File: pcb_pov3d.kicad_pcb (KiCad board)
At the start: 2 copper layers, 92 parts, among them P1 CONN_4X2, P2 CONN_6, P3 MICRO-SD, P4 CONN_2, P5 KNUSB, P6 CONN_12, U1 TLC5955, U2 TLC5955, U3 TLC5955, U4 STM32F40X_LQFP64, U5 US4881_HALL, U6 LP38691, X1 CRYSTAL

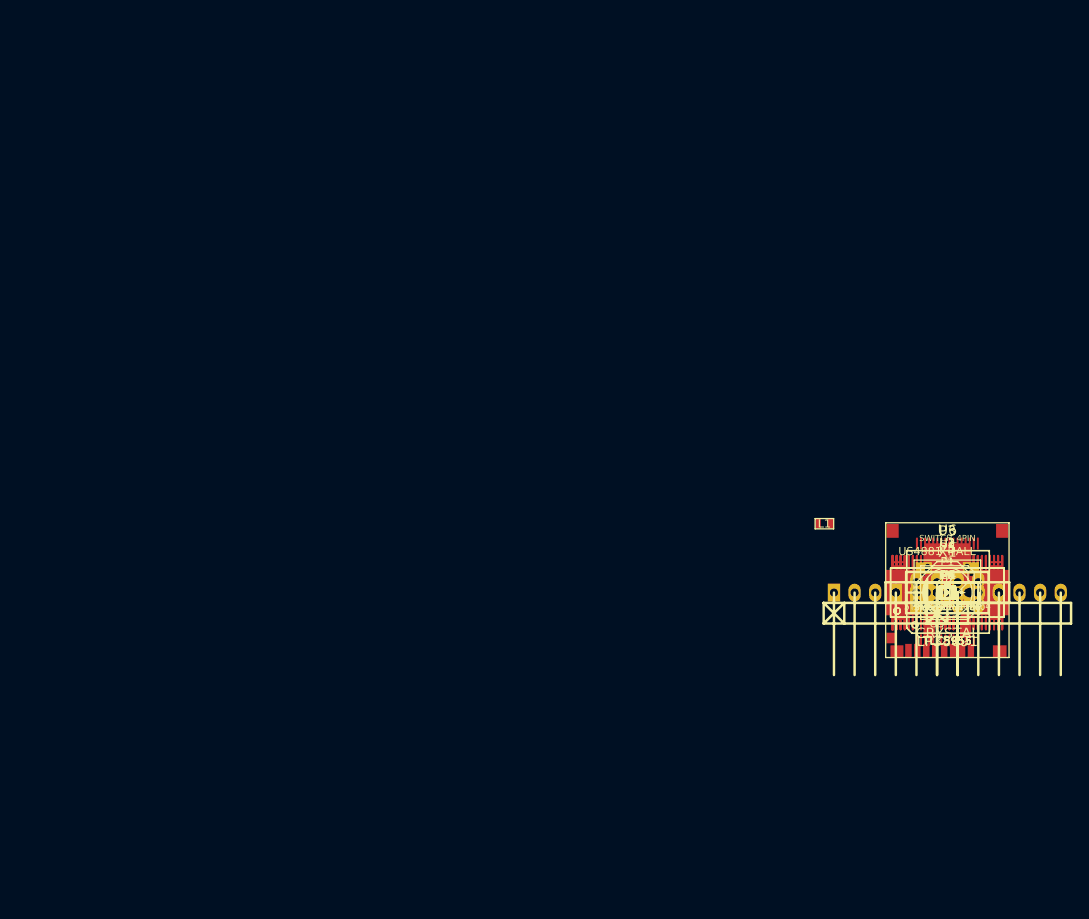
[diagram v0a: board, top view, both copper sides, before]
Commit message: Place RGB LEDs in the computed pattern for 3D POV effect.
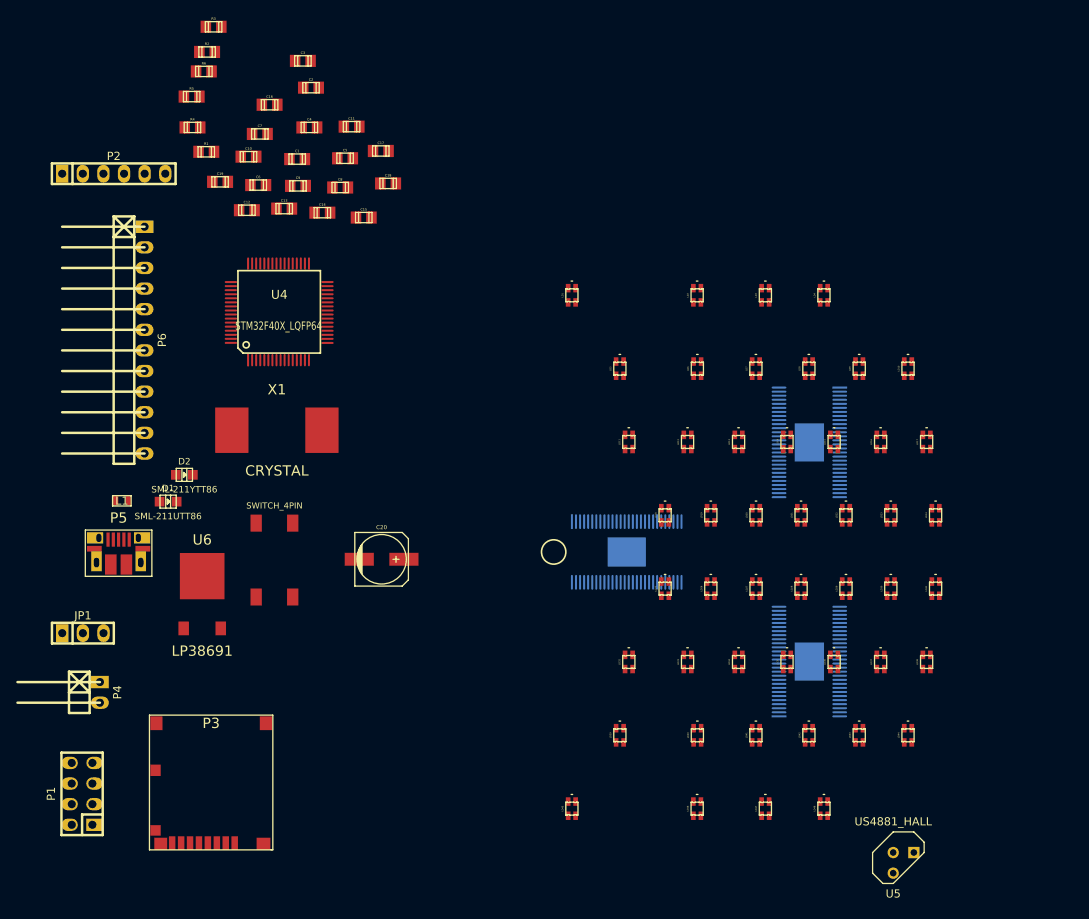
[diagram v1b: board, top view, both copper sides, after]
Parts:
- U1, U2, U3: moved to B.Cu
- moved P2 114.9 mm to (45.8, 53.4)
- moved R3 114.2 mm to (58.1, 35.3)
- moved R2 112.9 mm to (57.3, 38.4)
- moved R6 111.9 mm to (56.9, 40.8)
- moved R5 111.4 mm to (55.4, 43.9)
- moved P1 109.4 mm to (41.9, 129.8), turned to 90 degrees
- moved R4 109.2 mm to (55.5, 47.7)
- moved JP1 106.6 mm to (42.0, 110.0)
- moved R1 106.2 mm to (57.2, 50.7)
- moved P4 105.1 mm to (44.1, 117.3), turned to 270 degrees
- moved P6 103.7 mm to (49.6, 73.9), turned to 270 degrees
- moved C3 102.9 mm to (69.1, 39.5)
- moved C19 102.9 mm to (58.9, 54.4)
- moved C16 102.9 mm to (65.0, 44.9)
- moved P5 102.2 mm to (46.4, 101.3)
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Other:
- copper layers 2 -> 4
- net class Default: clearance 0.254 -> 0.2032; trace_width 0.254 -> 0.2032; via_dia 0.889 -> 0.635; via_drill 0.635 -> 0.3048
- net class Inner added: clearance 0.2032, trace_width 0.254, via_dia 0.635, via_drill 0.3048
- net class Tight added: clearance 0.1524, trace_width 0.1524, via_dia 0.635, via_drill 0.3048
- rule trace_clearance: 0.254 -> 0.2032
- rule trace_min: 0.254 -> 0.1524
- rule via_min_drill: 0.508 -> 0.3048
- rule via_min_size: 0.889 -> 0.635

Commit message: Assignment of LEDs to TLC5955 outputs.
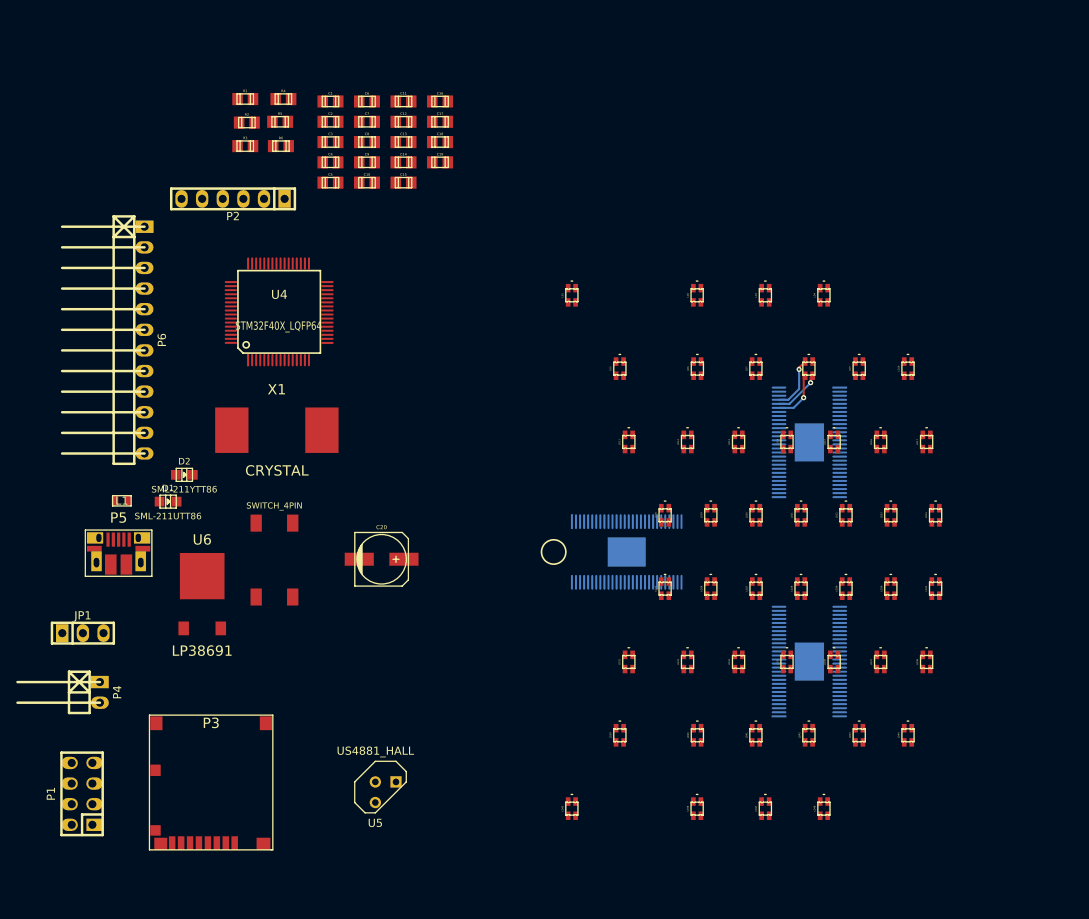
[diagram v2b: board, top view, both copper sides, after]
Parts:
- moved U5 64.4 mm to (79.3, 129.6)
- moved C19 27.2 mm to (86.0, 52.0)
- moved C12 22.2 mm to (81.5, 47.0)
- moved C16 21.0 mm to (86.0, 44.5)
- moved C6 16.9 mm to (77.0, 44.5)
- moved C13 16.8 mm to (81.5, 49.5)
- moved R3 15.2 mm to (62.0, 50.0)
- moved P2 15.0 mm to (60.5, 56.5), turned to 180 degrees
- moved C10 14.9 mm to (77.0, 54.5)
- moved C7 13.3 mm to (77.0, 47.0)
- moved R6 13.2 mm to (66.4, 50.0)
- moved C14 11.8 mm to (81.5, 52.0)
- moved R4 11.7 mm to (66.7, 44.2)
- moved R5 11.3 mm to (66.3, 47.0)
- moved C3 10.6 mm to (72.5, 49.5)
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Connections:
- U1 pad 10: /LEDs/t1o5b -> /LEDs/led15b
- U1 pad 11: /LEDs/t1o5r -> /LEDs/led15r
- U1 pad 12: /LEDs/t1o5g -> /LEDs/led15g
- U1 pad 13: /LEDs/t1o1b -> /LEDs/led16b
- U1 pad 14: /LEDs/t1o1r -> /LEDs/led16r
- U1 pad 15: /LEDs/t1o1g -> /LEDs/led16g
- U1 pad 16: /LEDs/t1o2b -> /LEDs/led17b
- U1 pad 17: /LEDs/t1o2r -> /LEDs/led17r
- U1 pad 18: /LEDs/t1o2g -> /LEDs/led17g
- U1 pad 19: /LEDs/t1o6b -> /LEDs/led24b
- U1 pad 20: /LEDs/t1o6r -> /LEDs/led24r
- U1 pad 21: /LEDs/t1o6g -> /LEDs/led24g
- U1 pad 22: /LEDs/t1o3b -> /LEDs/led23b
- U1 pad 23: /LEDs/t1o3r -> /LEDs/led23r
- U1 pad 24: /LEDs/t1o3g -> /LEDs/led23g
- U1 pad 25: /LEDs/t1o7b -> /LEDs/led22b
- U1 pad 26: /LEDs/t1o7r -> /LEDs/led22r
- U1 pad 27: /LEDs/t1o7g -> /LEDs/led22g
- U1 pad 30: /LEDs/t1o11g -> /LEDs/led21g
- U1 pad 31: /LEDs/t1o11r -> /LEDs/led21r
- U1 pad 32: /LEDs/t1o11b -> /LEDs/led21b
- U1 pad 33: /LEDs/t1o15g -> /LEDs/led20g
- U1 pad 34: /LEDs/t1o15r -> /LEDs/led20r
- U1 pad 35: /LEDs/t1o15b -> /LEDs/led20b
- U1 pad 36: /LEDs/t1o10g -> /LEDs/led13g
- U1 pad 37: /LEDs/t1o10r -> /LEDs/led13r
- U1 pad 38: /LEDs/t1o10b -> /LEDs/led13b
- U1 pad 39: /LEDs/t1o14g -> /LEDs/led7g
- U1 pad 4: /LEDs/t1o4b -> /LEDs/led9b
- U1 pad 40: /LEDs/t1o14r -> /LEDs/led7r
- U1 pad 41: /LEDs/t1o14b -> /LEDs/led7b
- U1 pad 42: /LEDs/t1o13g -> /LEDs/led14g
- U1 pad 43: /LEDs/t1o13r -> /LEDs/led14r
- U1 pad 44: /LEDs/t1o13b -> /LEDs/led14b
- U1 pad 45: /LEDs/t1o9g -> /LEDs/led4g
- U1 pad 46: /LEDs/t1o9r -> /LEDs/led4r
- U1 pad 47: /LEDs/t1o9b -> /LEDs/led4b
- U1 pad 48: /LEDs/t1o12g -> /LEDs/led3g
- U1 pad 49: /LEDs/t1o12r -> /LEDs/led3r
- U1 pad 5: /LEDs/t1o4r -> /LEDs/led9r
- U1 pad 50: /LEDs/t1o12b -> /LEDs/led3b
- U1 pad 51: /LEDs/t1o8g -> /LEDs/led8g
- U1 pad 52: /LEDs/t1o8r -> /LEDs/led8r
- U1 pad 53: /LEDs/t1o8b -> /LEDs/led8b
- U1 pad 6: /LEDs/t1o4g -> /LEDs/led9g
- U1 pad 7: /LEDs/t1o0b -> /LEDs/led10b
- U1 pad 8: /LEDs/t1o0r -> /LEDs/led10r
- U1 pad 9: /LEDs/t1o0g -> /LEDs/led10g
- U2 pad 10: /LEDs/t2o5b -> /LEDs/led11b
- U2 pad 11: /LEDs/t2o5r -> /LEDs/led11r
- U2 pad 12: /LEDs/t2o5g -> /LEDs/led11g
- U2 pad 13: /LEDs/t2o1b -> /LEDs/led2b
- U2 pad 14: /LEDs/t2o1r -> /LEDs/led2r
- U2 pad 15: /LEDs/t2o1g -> /LEDs/led2g
- U2 pad 16: /LEDs/t2o2b -> /LEDs/led6b
- U2 pad 17: /LEDs/t2o2r -> /LEDs/led6r
- U2 pad 18: /LEDs/t2o2g -> /LEDs/led6g
- U2 pad 19: /LEDs/t2o6b -> /LEDs/led12b
- U2 pad 20: /LEDs/t2o6r -> /LEDs/led12r
- U2 pad 21: /LEDs/t2o6g -> /LEDs/led12g
- U2 pad 22: /LEDs/t2o3b -> /LEDs/led18b
- U2 pad 23: /LEDs/t2o3r -> /LEDs/led18r
- U2 pad 24: /LEDs/t2o3g -> /LEDs/led18g
- U2 pad 25: /LEDs/t2o7b -> /LEDs/led19b
- U2 pad 26: /LEDs/t2o7r -> /LEDs/led19r
- U2 pad 27: /LEDs/t2o7g -> /LEDs/led19g
- U2 pad 30: /LEDs/t2o11g -> /LEDs/led26g
- U2 pad 31: /LEDs/t2o11r -> /LEDs/led26r
- U2 pad 32: /LEDs/t2o11b -> /LEDs/led26b
- U2 pad 33: /LEDs/t2o15g -> /LEDs/led25g
- U2 pad 34: /LEDs/t2o15r -> /LEDs/led25r
- U2 pad 35: /LEDs/t2o15b -> /LEDs/led25b
- U2 pad 36: /LEDs/t2o10g -> /LEDs/led33g
- U2 pad 37: /LEDs/t2o10r -> /LEDs/led33r
- U2 pad 38: /LEDs/t2o10b -> /LEDs/led33b
- U2 pad 39: /LEDs/t2o14g -> /LEDs/led40g
- U2 pad 4: /LEDs/t2o4b -> /LEDs/led1b
- U2 pad 40: /LEDs/t2o14r -> /LEDs/led40r
- U2 pad 41: /LEDs/t2o14b -> /LEDs/led40b
- U2 pad 42: /LEDs/t2o13g -> /LEDs/led46g
- U2 pad 43: /LEDs/t2o13r -> /LEDs/led46r
- U2 pad 44: /LEDs/t2o13b -> /LEDs/led46b
- U2 pad 45: /LEDs/t2o9g -> /LEDs/led32g
- U2 pad 46: /LEDs/t2o9r -> /LEDs/led32r
- U2 pad 47: /LEDs/t2o9b -> /LEDs/led32b
- U2 pad 48: /LEDs/t2o12g -> /LEDs/led39g
- U2 pad 49: /LEDs/t2o12r -> /LEDs/led39r
- U2 pad 5: /LEDs/t2o4r -> /LEDs/led1r
- U2 pad 50: /LEDs/t2o12b -> /LEDs/led39b
- U2 pad 51: /LEDs/t2o8g -> /LEDs/led45g
- U2 pad 52: /LEDs/t2o8r -> /LEDs/led45r
- U2 pad 53: /LEDs/t2o8b -> /LEDs/led45b
- U2 pad 6: /LEDs/t2o4g -> /LEDs/led1g
- U2 pad 7: /LEDs/t2o0b -> /LEDs/led5b
- U2 pad 8: /LEDs/t2o0r -> /LEDs/led5r
- U2 pad 9: /LEDs/t2o0g -> /LEDs/led5g
- U3 pad 10: /LEDs/t3o5b -> /LEDs/led48b
- U3 pad 11: /LEDs/t3o5r -> /LEDs/led48r
- U3 pad 12: /LEDs/t3o5g -> /LEDs/led48g
- U3 pad 13: /LEDs/t3o1b -> /LEDs/led35b
- U3 pad 14: /LEDs/t3o1r -> /LEDs/led35r
- U3 pad 15: /LEDs/t3o1g -> /LEDs/led35g
- U3 pad 16: /LEDs/t3o2b -> /LEDs/led41b
- U3 pad 17: /LEDs/t3o2r -> /LEDs/led41r
- U3 pad 18: /LEDs/t3o2g -> /LEDs/led41g
- U3 pad 19: /LEDs/t3o6b -> /LEDs/led34b
- U3 pad 20: /LEDs/t3o6r -> /LEDs/led34r
- U3 pad 21: /LEDs/t3o6g -> /LEDs/led34g
- U3 pad 22: /LEDs/t3o3b -> /LEDs/led27b
- U3 pad 23: /LEDs/t3o3r -> /LEDs/led27r
- U3 pad 24: /LEDs/t3o3g -> /LEDs/led27g
- U3 pad 25: /LEDs/t3o7b -> /LEDs/led28b
- U3 pad 26: /LEDs/t3o7r -> /LEDs/led28r
- U3 pad 27: /LEDs/t3o7g -> /LEDs/led28g
- U3 pad 30: /LEDs/t3o11g -> /LEDs/led29g
- U3 pad 31: /LEDs/t3o11r -> /LEDs/led29r
- U3 pad 32: /LEDs/t3o11b -> /LEDs/led29b
- U3 pad 33: /LEDs/t3o15g -> /LEDs/led30g
- U3 pad 34: /LEDs/t3o15r -> /LEDs/led30r
- U3 pad 35: /LEDs/t3o15b -> /LEDs/led30b
- U3 pad 36: /LEDs/t3o10g -> /LEDs/led31g
- U3 pad 37: /LEDs/t3o10r -> /LEDs/led31r
- U3 pad 38: /LEDs/t3o10b -> /LEDs/led31b
- U3 pad 39: /LEDs/t3o14g -> /LEDs/led38g
- U3 pad 4: /LEDs/t3o4b -> /LEDs/led42b
- U3 pad 40: /LEDs/t3o14r -> /LEDs/led38r
- U3 pad 41: /LEDs/t3o14b -> /LEDs/led38b
- U3 pad 42: /LEDs/t3o13g -> /LEDs/led37g
- U3 pad 43: /LEDs/t3o13r -> /LEDs/led37r
- U3 pad 44: /LEDs/t3o13b -> /LEDs/led37b
- U3 pad 45: /LEDs/t3o9g -> /LEDs/led36g
- U3 pad 46: /LEDs/t3o9r -> /LEDs/led36r
- U3 pad 47: /LEDs/t3o9b -> /LEDs/led36b
- U3 pad 48: /LEDs/t3o12g -> /LEDs/led44g
- U3 pad 49: /LEDs/t3o12r -> /LEDs/led44r
- U3 pad 5: /LEDs/t3o4r -> /LEDs/led42r
- U3 pad 50: /LEDs/t3o12b -> /LEDs/led44b
- U3 pad 51: /LEDs/t3o8g -> /LEDs/led43g
- U3 pad 52: /LEDs/t3o8r -> /LEDs/led43r
- U3 pad 53: /LEDs/t3o8b -> /LEDs/led43b
- U3 pad 6: /LEDs/t3o4g -> /LEDs/led42g
- U3 pad 7: /LEDs/t3o0b -> /LEDs/led47b
- U3 pad 8: /LEDs/t3o0r -> /LEDs/led47r
- U3 pad 9: /LEDs/t3o0g -> /LEDs/led47g
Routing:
- net /LEDs/led8b: track 0.00 -> 6.72 mm, vias 0 -> 1
- net /LEDs/led8g: track 0.00 -> 6.34 mm, vias 0 -> 1
- net /LEDs/led8r: track 0.00 -> 5.94 mm, vias 0 -> 1

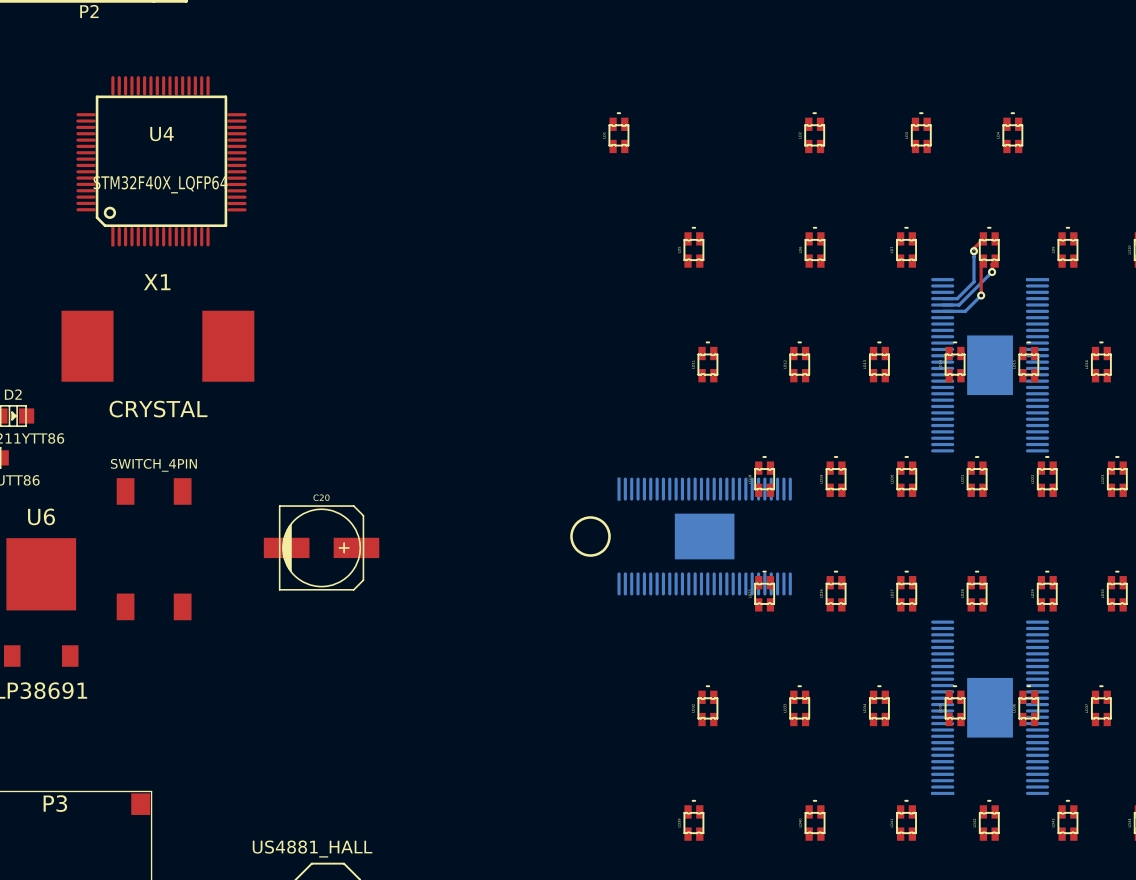
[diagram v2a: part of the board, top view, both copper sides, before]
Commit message: Powerpads on TLC5955's, and sketch of high-speed signals routing.
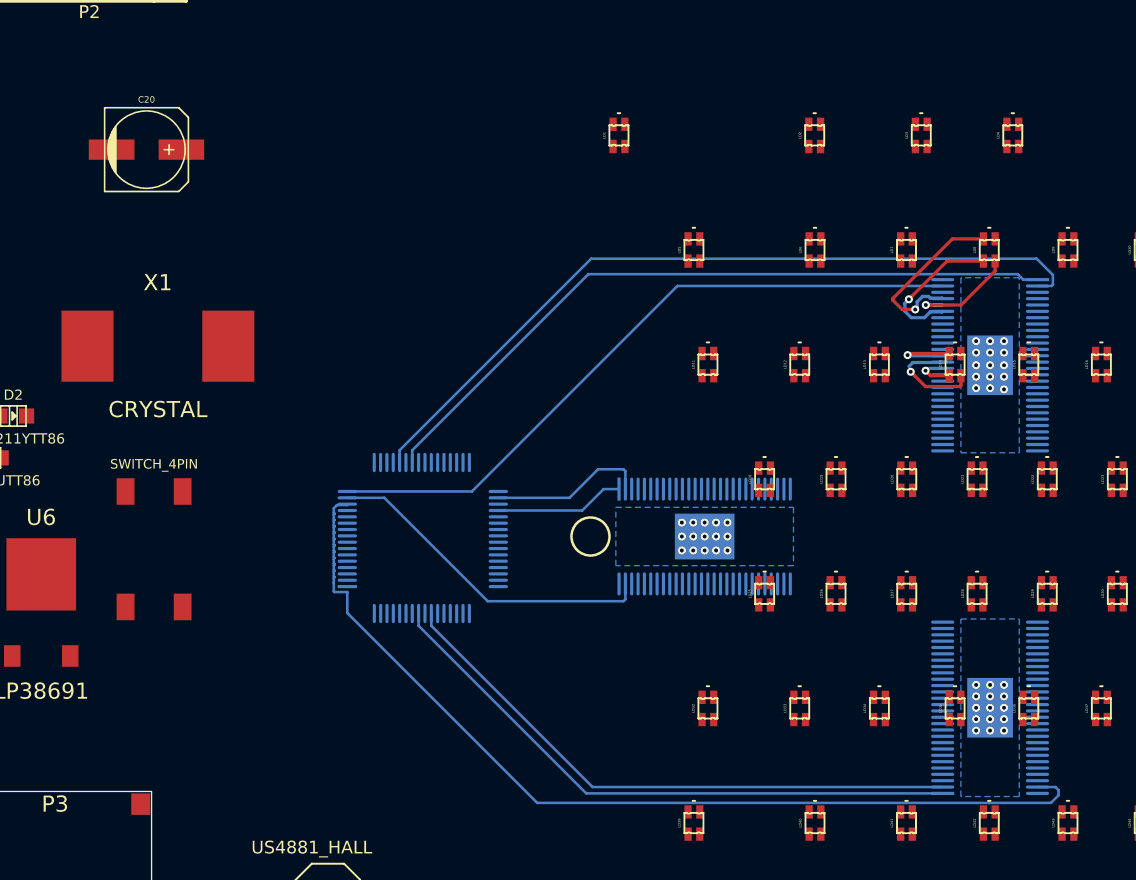
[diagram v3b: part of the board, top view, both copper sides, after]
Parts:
- U4: moved to B.Cu
- moved U4 36.1 mm to (86.7, 100.2), turned to 90 degrees
- moved C20 34.3 mm to (65.0, 69.5)
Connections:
- U4 pad 14: /LEDs/gsclk1 -> /LEDs/gsclk3
- U4 pad 16: /LEDs/gsclk3 -> /LEDs/gsclk1
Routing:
- net /LEDs/gsclk3: track 0.00 -> 75.9 mm
- net /LEDs/sclk1: track 0.00 -> 61.3 mm
- net /LEDs/sin1: track 0.00 -> 56.2 mm
- net /LEDs/gsclk1: track 0.00 -> 53.6 mm
- net /LEDs/sin3: track 0.00 -> 47.8 mm
- net /LEDs/sclk3: track 0.00 -> 46.5 mm
- net /LEDs/gsclk2: track 0.00 -> 26.6 mm
- net /LEDs/sclk2: track 0.00 -> 12.4 mm
- net /LEDs/sin2: track 0.00 -> 10.2 mm
- net /LEDs/led14r: track 0.00 -> 8.06 mm, vias 0 -> 1
- net /LEDs/led8b: track 6.72 -> 14.2 mm
- net /LEDs/led14b: track 0.00 -> 6.12 mm, vias 0 -> 1
- net /LEDs/led8g: track 6.34 -> 11.6 mm
- net /LEDs/led14g: track 0.00 -> 3.45 mm, vias 0 -> 1
- net /LEDs/led8r: track 5.94 -> 8.68 mm
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- added copper zone on B.Cu, net GND
